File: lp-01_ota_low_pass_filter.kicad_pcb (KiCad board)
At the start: 2 copper layers, 38.3 x 100 mm, 52 parts, among them J1 AudioJack2, J2 AudioJack2, J3 AudioJack2, J4 AudioJack2, J5 Conn_02x05_Odd_Even, Q1 2N3906, Q2 2N3906, U1 TL072, U2 LM13700, U3 TL074

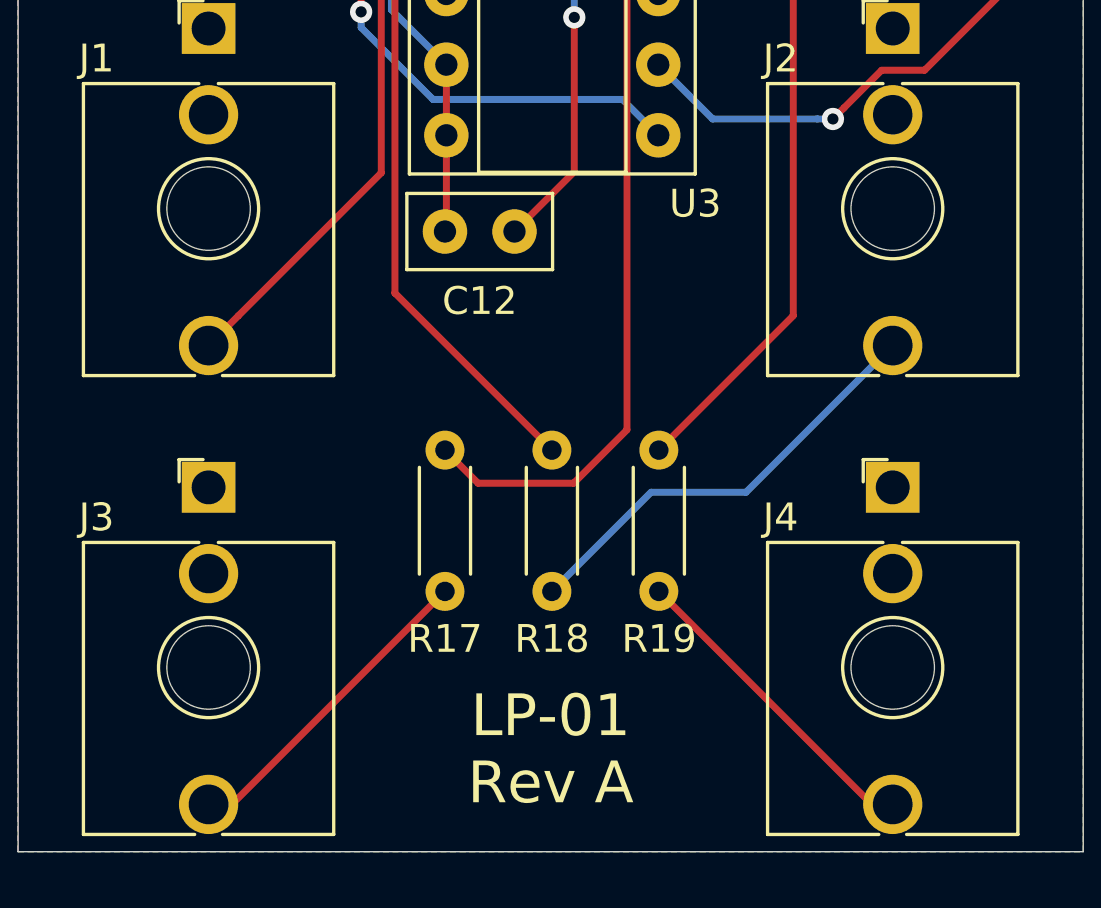
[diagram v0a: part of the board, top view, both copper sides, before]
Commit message: Revision A.2
- A few small component tweaks
- Add OSHW logos
- Prepare for public release?
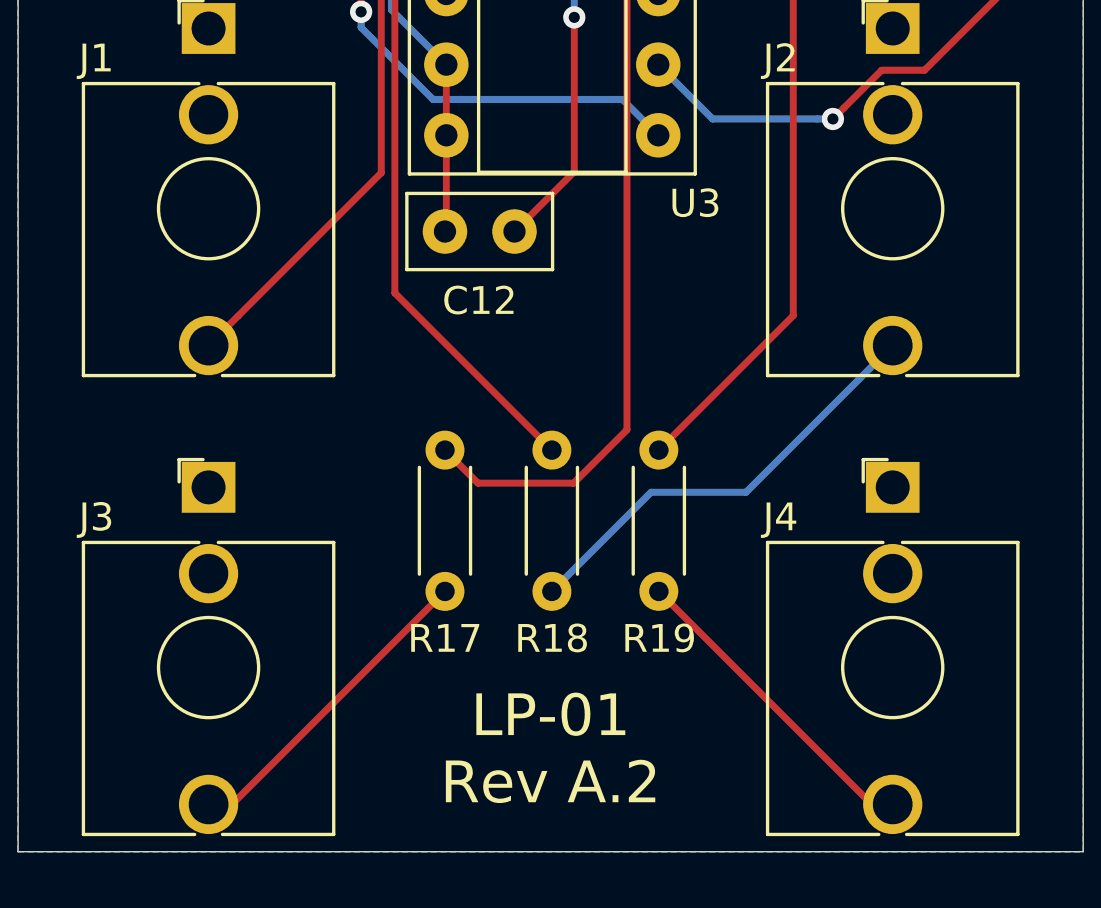
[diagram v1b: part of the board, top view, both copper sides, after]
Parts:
- removed REF** (x4): MountingHole_3mm, MountingHole:MountingHole_3mm
- added LOGO1: Logo_Open_Hardware_Large, Symbol:OSHW-Logo_5.7x6mm_SilkScreen, B.Cu at (140.2, 144.8)
- R1: value 4K7 -> 47K
- R18: value 100K -> 220K
- RV1, RV4: value B10K -> B100K
- RV5: value A100K -> B100K
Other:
- board text added: "20121227 RJH"
- board text added: "LP-01 Rev A.2"
- board text added: "Rev A.2"
- board text added: "robhailman.com"
- board text removed: "20190912 RJH"
- board text removed: "LP-01 Rev A"
- board text removed: "Rev A"

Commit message: Revert RV5 to log pot
This works much better!
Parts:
- RV5: value B100K -> A100K
